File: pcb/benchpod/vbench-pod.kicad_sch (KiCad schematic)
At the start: 112 parts, among them J1 PZ254V-12-22P, SW1 TS-1088-AR02016, SW2 TS-1088-AR02016, U1 ICE40UP5K-SG48ITR, U10 TCAN1044VDRBRQ1, U2 W25Q64JVSSIQ, U24 SN74LVC2G66DCUR, U4 ESP32-C3-MINI-1-N4, U5 STM32H563ZIT6, U7 APS6404L-3SQR-ZR, U8 TPS2116DRLR, X1 SX3M48.000B10F20TNN, Y2 Crystal_GND24

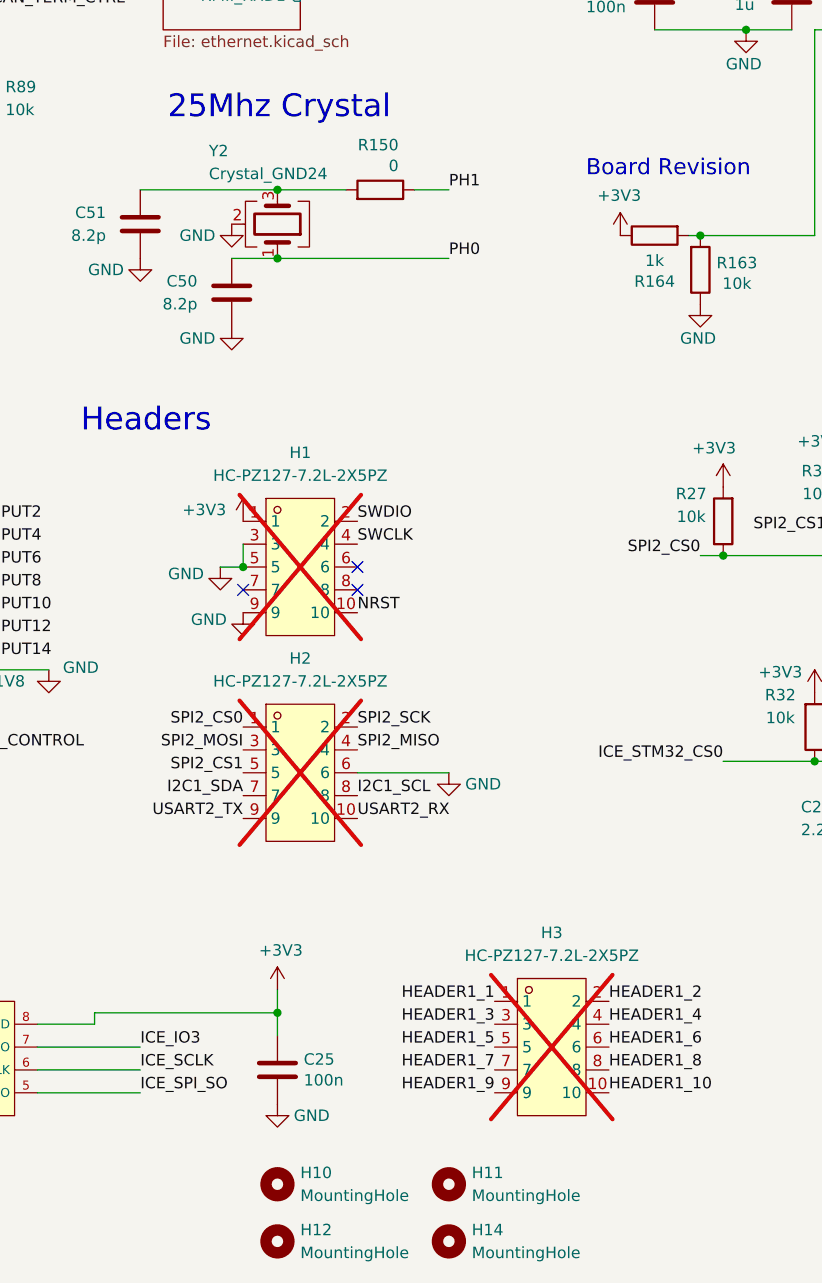
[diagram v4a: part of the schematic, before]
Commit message: replace d1, cleanups, cap changes
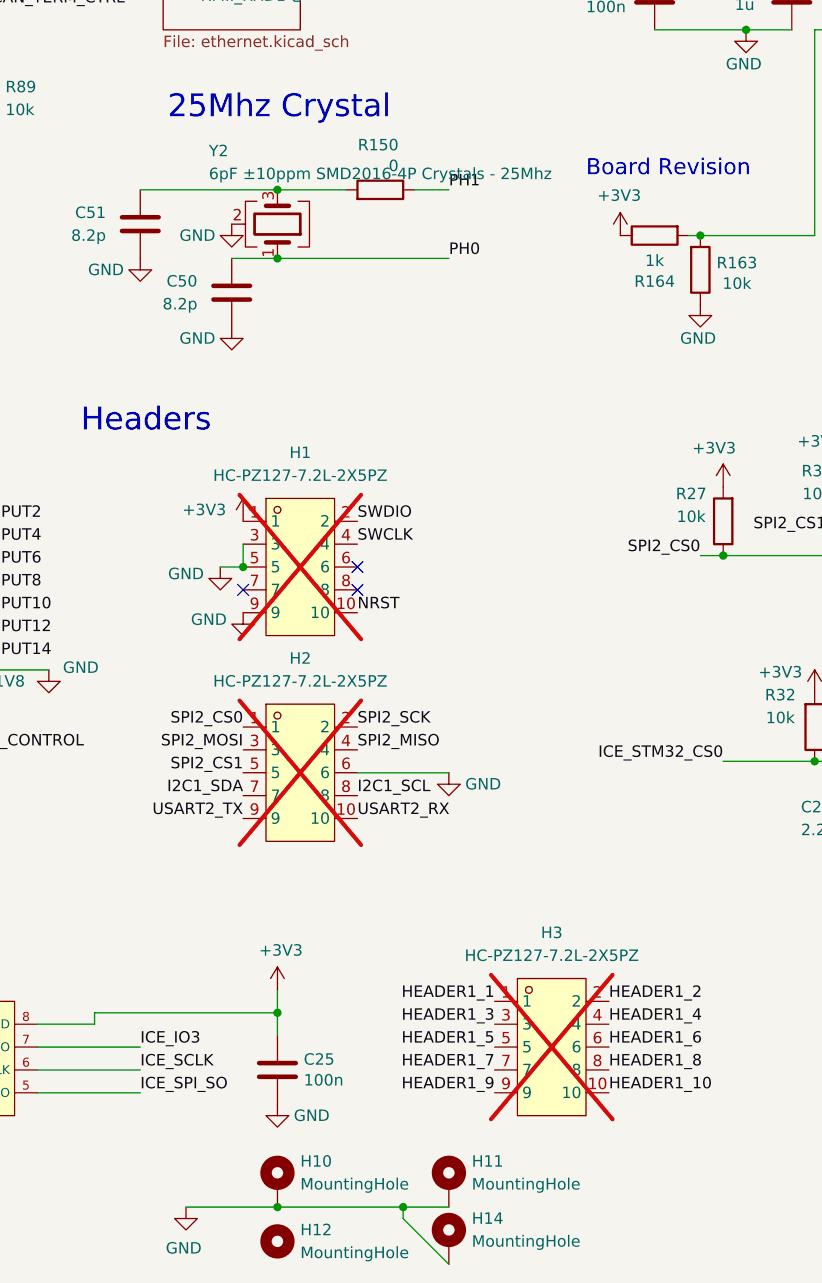
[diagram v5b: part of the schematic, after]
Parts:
- C2, C3: footprint Capacitor_SMD:C_0603_1608Metric -> Capacitor_SMD:C_0805_2012Metric; LCSC C19666 -> C98192
- C220: footprint Capacitor_SMD:C_1206_3216Metric -> Capacitor_SMD:C_0805_2012Metric; LCSC C29823 -> C98192
- H10, H11, H14: footprint MountingHole:MountingHole_2.7mm_M2.5 -> MountingHole:MountingHole_2.7mm_M2.5_Pad_Via; symbol Mechanical:MountingHole -> Mechanical:MountingHole_Pad
- Y2: value Crystal_GND24 -> 6pF ±10ppm SMD2016-4P Crystals - 25Mhz
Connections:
- net GND: now also H10.1, H11.1, H14.1
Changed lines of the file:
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@@
 	)
 	(junction
+		(at 246.38 275.59)
+		(diameter 0)
+		(color 0 0 0 0)
+	)
+	(junction
+		(at 260.35 275.59)
+		(diameter 0)
+		(color 0 0 0 0)
+	)
+	(junction
 		(at 323.85 36.83)
 		(diameter 0)
@@
 	(wire
 		(pts
+			(xy 236.22 275.59) (xy 246.38 275.59)
+		)
+		(stroke
+			(width 0)
+			(type default)
+		)
+	)
+	(wire
+		(pts
 			(xy 40.64 224.79) (xy 39.37 224.79)
 		)
@@
 	(wire
 		(pts
+			(xy 260.35 275.59) (xy 265.43 275.59)
+		)
+		(stroke
+			(width 0)
+			(type default)
+		)
+	)
+	(wire
+		(pts
 			(xy 196.85 62.23) (xy 196.85 64.77)
 		)
@@
 	(wire
 		(pts
+			(xy 246.38 275.59) (xy 260.35 275.59)
+		)
+		(stroke
+			(width 0)
+			(type default)
+		)
+	)
+	(wire
+		(pts
 			(xy 306.07 226.06) (xy 330.2 226.06)
 		)
@@
 	(wire
 		(pts
+			(xy 265.43 281.94) (xy 260.35 276.86)
+		)
+		(stroke
+			(width 0)
+			(type default)
+		)
+	)
+	(wire
+		(pts
 			(xy 312.42 36.83) (xy 323.85 36.83)
 		)
@@
 	(wire
 		(pts
+			(xy 260.35 275.59) (xy 260.35 276.86)
+		)
+		(stroke
+			(width 0)
+			(type default)
+		)
+	)
+	(wire
+		(pts
 			(xy 219.71 255.27) (xy 226.06 255.27)
 		)
@@
 	)
 	(symbol
-		(lib_id "Mechanical:MountingHole")
+		(lib_id "Mechanical:MountingHole_Pad")
 		(at 265.43 273.05 0)
 		(unit 1)
@@
 		(fields_autoplaced yes)
 		(property "Reference" "H11"
-			(at 267.97 271.7799 0)
+			(at 267.97 270.5099 0)
 			(show_name no)
 			(do_not_autoplace no)
@@
 		)
 		(property "Value" "MountingHole"
-			(at 267.97 274.3199 0)
+			(at 267.97 273.0499 0)
 			(show_name no)
 			(do_not_autoplace no)
@@
 			)
 		)
-		(property "Footprint" "MountingHole:MountingHole_2.7mm_M2.5"
+		(property "Footprint" "MountingHole:MountingHole_2.7mm_M2.5_Pad_Via"
 			(at 265.43 273.05 0)
 			(hide yes)
@@
 			)
 		)
-		(property "Description" "Mounting Hole without connection"
+		(property "Description" "Mounting Hole with connection"
 			(at 265.43 273.05 0)
 			(hide yes)
@@
 			)
 		)
+		(pin "1"
+		)
 		(instances
 			(project "vbench-pod"
@@
 	)
 	(symbol
+		(lib_id "power:GND")
+		(at 236.22 275.59 0)
+		(unit 1)
+		(body_style 1)
+		(exclude_from_sim no)
+		(in_bom yes)
+		(on_board yes)
+		(in_pos_files yes)
+		(dnp no)
+		(property "Reference" "#PWR064"
+			(at 236.22 281.94 0)
+			(hide yes)
+			(show_name no)
+			(do_not_autoplace no)
+			(effects
+				(font
+					(size 1.27 1.27)
+				)
+			)
+		)
+		(property "Value" "GND"
+			(at 235.966 280.162 0)
+			(show_name no)
+			(do_not_autoplace no)
+			(effects
+				(font
+					(size 1.27 1.27)
+				)
+			)
+		)
+		(property "Footprint" ""
+			(at 236.22 275.59 0)
+			(hide yes)
+			(show_name no)
+			(do_not_autoplace no)
+			(effects
+				(font
+					(size 1.27 1.27)
+				)
+			)
+		)
+		(property "Datasheet" ""
+			(at 236.22 275.59 0)
+			(hide yes)
+			(show_name no)
+			(do_not_autoplace no)
+			(effects
+				(font
+					(size 1.27 1.27)
+				)
+			)
+		)
+		(property "Description" ""
+			(at 236.22 275.59 0)
+			(show_name no)
+			(do_not_autoplace no)
+			(effects
+				(font
+					(size 1.27 1.27)
+				)
+			)
+		)
+		(pin "1"
+		)
+		(instances
+			(project "vbench-pod"
+				(path "/745fcf4b-2e0b-4fc4-95c0-f2e3fd40beb9"
+					(reference "#PWR064")
+					(unit 1)
+				)
+			)
+		)
+	)
+	(symbol
 		(lib_id "Device:C")
 		(at 142.24 30.48 0)
@@
 			)
 		)
-		(property "Footprint" "Capacitor_SMD:C_1206_3216Metric"
+		(property "Footprint" "Capacitor_SMD:C_0805_2012Metric"
 			(at 244.8052 36.83 0)
 			(hide yes)
@@
 			)
 		)
-		(property "LCSC" "C29823"
+		(property "LCSC" "C98192"
 			(at 243.84 33.02 0)
 			(hide yes)
@@
 			)
 		)
-		(property "Footprint" "Capacitor_SMD:C_0603_1608Metric"
+		(property "Footprint" "Capacitor_SMD:C_0805_2012Metric"
 			(at 25.7048 149.86 0)
 			(hide yes)
@@
 			)
 		)
-		(property "LCSC" "C19666"
+		(property "LCSC" "C98192"
 			(at 26.67 146.05 0)
 			(hide yes)
@@
 			)
 		)
-		(property "Value" "Crystal_GND24"
+		(property "Value" "6pF ±10ppm SMD2016-4P Crystals  - 25Mhz"
 			(at 238.76 160.782 90)
 			(show_name no)
@@
 	)
 	(symbol
-		(lib_id "Mechanical:MountingHole")
+		(lib_id "Mechanical:MountingHole_Pad")
 		(at 265.43 279.4 0)
 		(unit 1)
@@
 		(fields_autoplaced yes)
 		(property "Reference" "H14"
-			(at 267.97 278.1299 0)
+			(at 267.97 276.8599 0)
 			(show_name no)
 			(do_not_autoplace no)
@@
 		)
 		(property "Value" "MountingHole"
-			(at 267.97 280.6699 0)
+			(at 267.97 279.3999 0)
 			(show_name no)
 			(do_not_autoplace no)
@@
 			)
 		)
-		(property "Footprint" "MountingHole:MountingHole_2.7mm_M2.5"
+		(property "Footprint" "MountingHole:MountingHole_2.7mm_M2.5_Pad_Via"
 			(at 265.43 279.4 0)
 			(hide yes)
@@
 			)
 		)
-		(property "Description" "Mounting Hole without connection"
+		(property "Description" "Mounting Hole with connection"
 			(at 265.43 279.4 0)
 			(hide yes)
@@
 			)
 		)
+		(pin "1"
+		)
 		(instances
 			(project "vbench-pod"
@@
 	)
 	(symbol
-		(lib_id "Mechanical:MountingHole")
+		(lib_id "Mechanical:MountingHole_Pad")
 		(at 246.38 273.05 0)
 		(unit 1)
@@
 		(fields_autoplaced yes)
 		(property "Reference" "H10"
-			(at 248.92 271.7799 0)
+			(at 248.92 270.5099 0)
 			(show_name no)
 			(do_not_autoplace no)
@@
 		)
 		(property "Value" "MountingHole"
-			(at 248.92 274.3199 0)
+			(at 248.92 273.0499 0)
 			(show_name no)
 			(do_not_autoplace no)
@@
 			)
 		)
-		(property "Footprint" "MountingHole:MountingHole_2.7mm_M2.5"
+		(property "Footprint" "MountingHole:MountingHole_2.7mm_M2.5_Pad_Via"
 			(at 246.38 273.05 0)
 			(hide yes)
@@
 			)
 		)
-		(property "Description" "Mounting Hole without connection"
+		(property "Description" "Mounting Hole with connection"
 			(at 246.38 273.05 0)
 			(hide yes)
@@
 			)
 		)
+		(pin "1"
+		)
 		(instances
 			(project "vbench-pod"
@@
 			)
 		)
-		(property "Footprint" "Capacitor_SMD:C_0603_1608Metric"
+		(property "Footprint" "Capacitor_SMD:C_0805_2012Metric"
 			(at 28.2448 135.89 0)
 			(hide yes)
@@
 			)
 		)
-		(property "LCSC" "C19666"
+		(property "LCSC" "C98192"
 			(at 29.21 132.08 0)
 			(hide yes)

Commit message: 5VA->5V for relays, resistor and cap changes
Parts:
- removed C59: 100n, Capacitor_SMD:C_0402_1005Metric, symbol Device:C
- removed FB1: FerriteBead, lcsc:L0603, symbol Device:FerriteBead
- added C66: 10u, Capacitor_SMD:C_0603_1608Metric, symbol Device:C
- added C97: 100n, Capacitor_SMD:C_0402_1005Metric, symbol Device:C
- added R174: 330, Resistor_SMD:R_0402_1005Metric, symbol Device:R
- added R175: 1k, Resistor_SMD:R_0402_1005Metric, symbol Device:R
- added R176: 56, Resistor_SMD:R_0402_1005Metric, symbol Device:R
- added R177: 100, Resistor_SMD:R_0402_1005Metric, symbol Device:R
- added U28: SRV05-4.TCT, lcsc:SOT-23-6_L2.9-W1.6-P0.95-LS2.8-BR, symbol edward_lib:SRV05-4.TCT
- C5: value 1u -> 4.7u; footprint Capacitor_SMD:C_0402_1005Metric -> Capacitor_SMD:C_0805_2012Metric; KiLib_Generator SMD_2terminal_chip_molded -> (none); LCSC C1518208 -> C98192; MPN CL21B105KBFNNNE -> (none)
- R18: value 120 -> 56; LCSC C25079 -> C25127
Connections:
- net +3V3: now also U8.5 (MODE), C97.2, U28.5
- net 1V2: now also C48.2, U1.30 (VCC), U1.5 (VCC), R177.2
- net CAN+: now also R176.1; no longer U24.1 (1A)
- net GND: now also C66.2, C97.1, R175.1, U28.2; no longer U8.5 (MODE)
- net LA_VCCIO: now also C66.1, R175.2
- net NRST_CONTROL: now also R174.1, U28.3; no longer U5.14 (PF4)
- net at C5.2, C6.2, U1.29 (VCCPLL): now also R177.1; no longer C48.2, U1.30 (VCC), U1.5 (VCC)
- net PD7: no longer names the net of U5.123 (PD7)
- net PG10: no longer names the net of U5.125 (PG10)
- net PG9: no longer names the net of U5.124 (PG9)
- new net: R174.2, U5.14 (PF4)
- new net: R176.2, U24.1 (1A)
- no-connect marks 56 -> 62
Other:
- note added: "bleeder resistor"
- moved on the sheet: C1, C2, C3, C4, C5, C6, J1

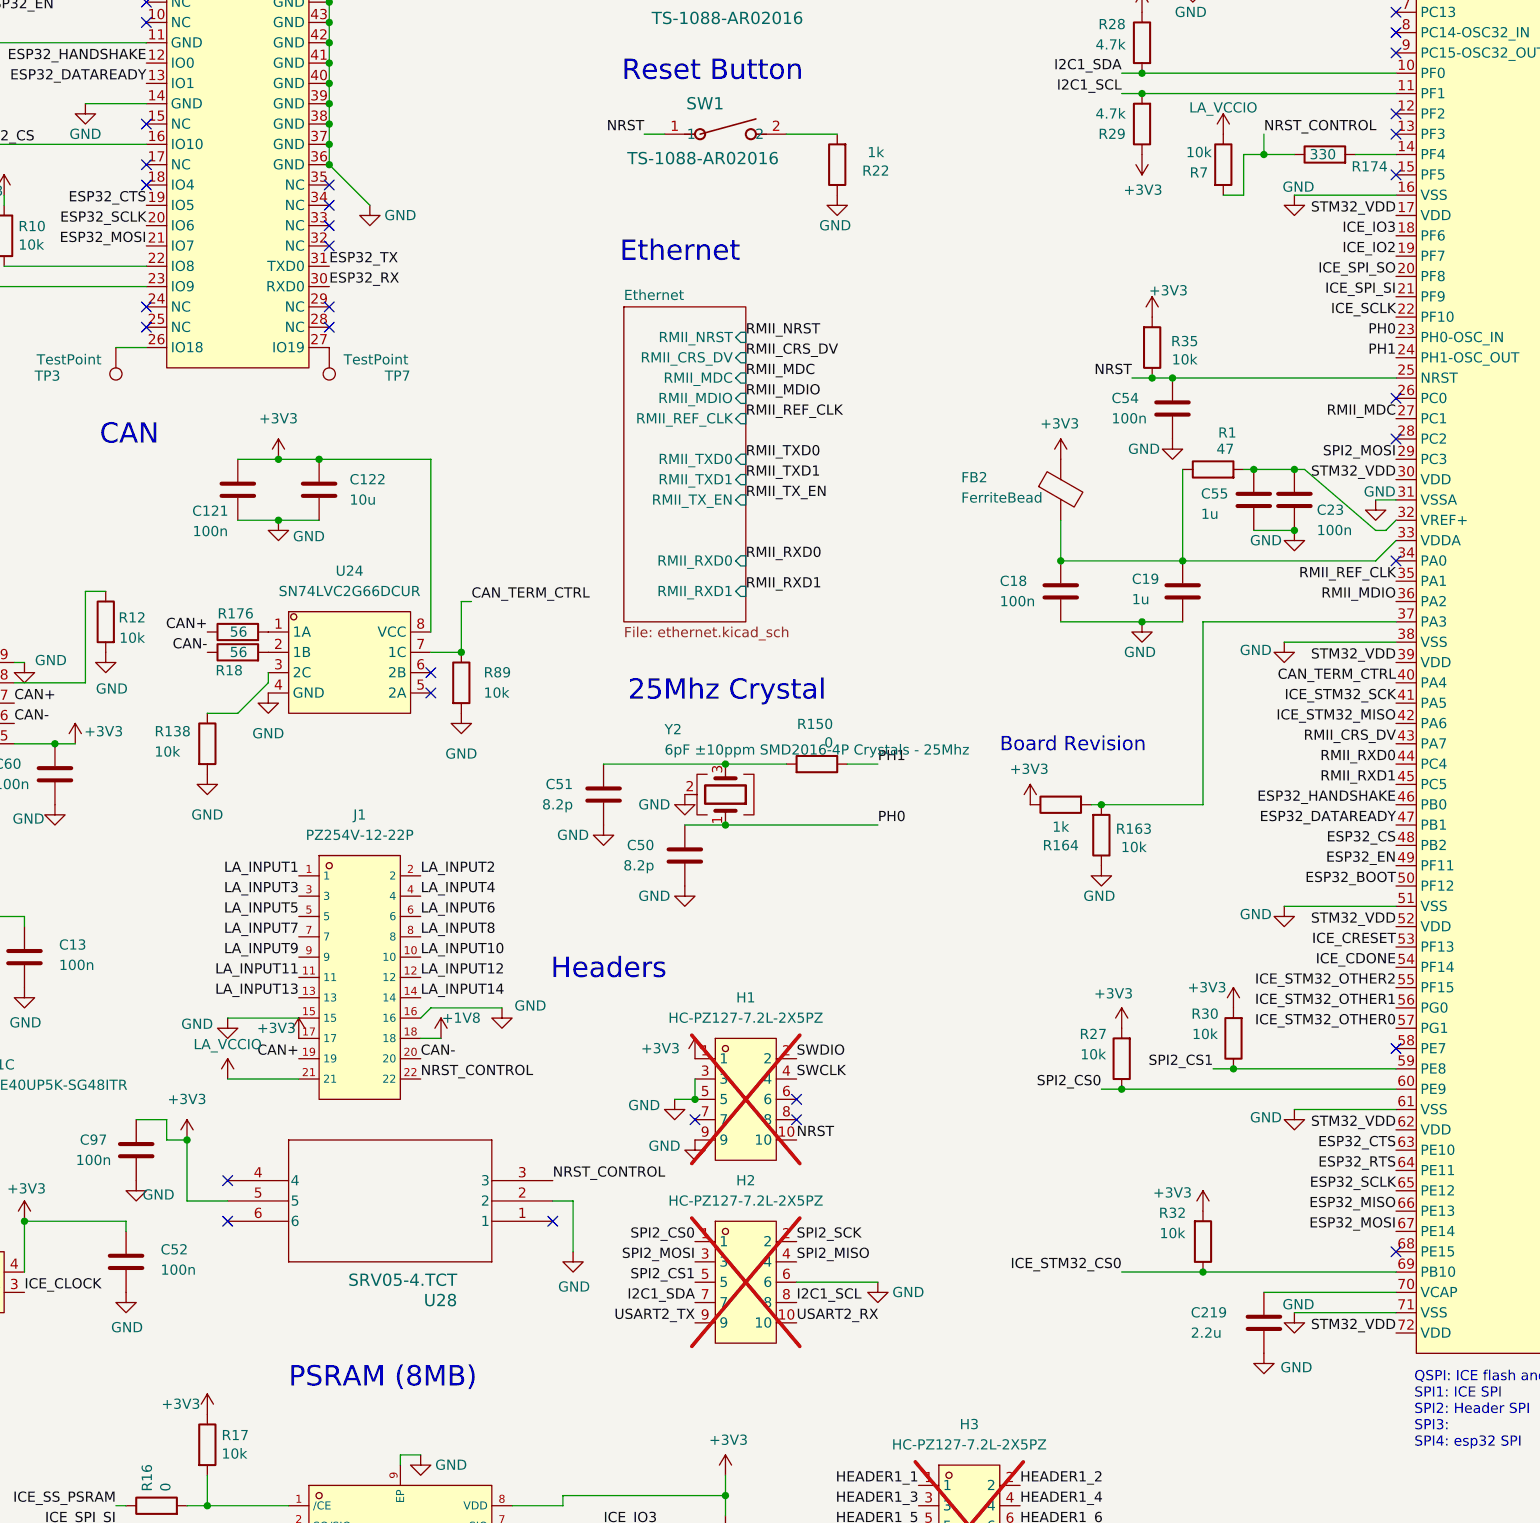
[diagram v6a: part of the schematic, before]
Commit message: 5VA->5V for relays rerouting
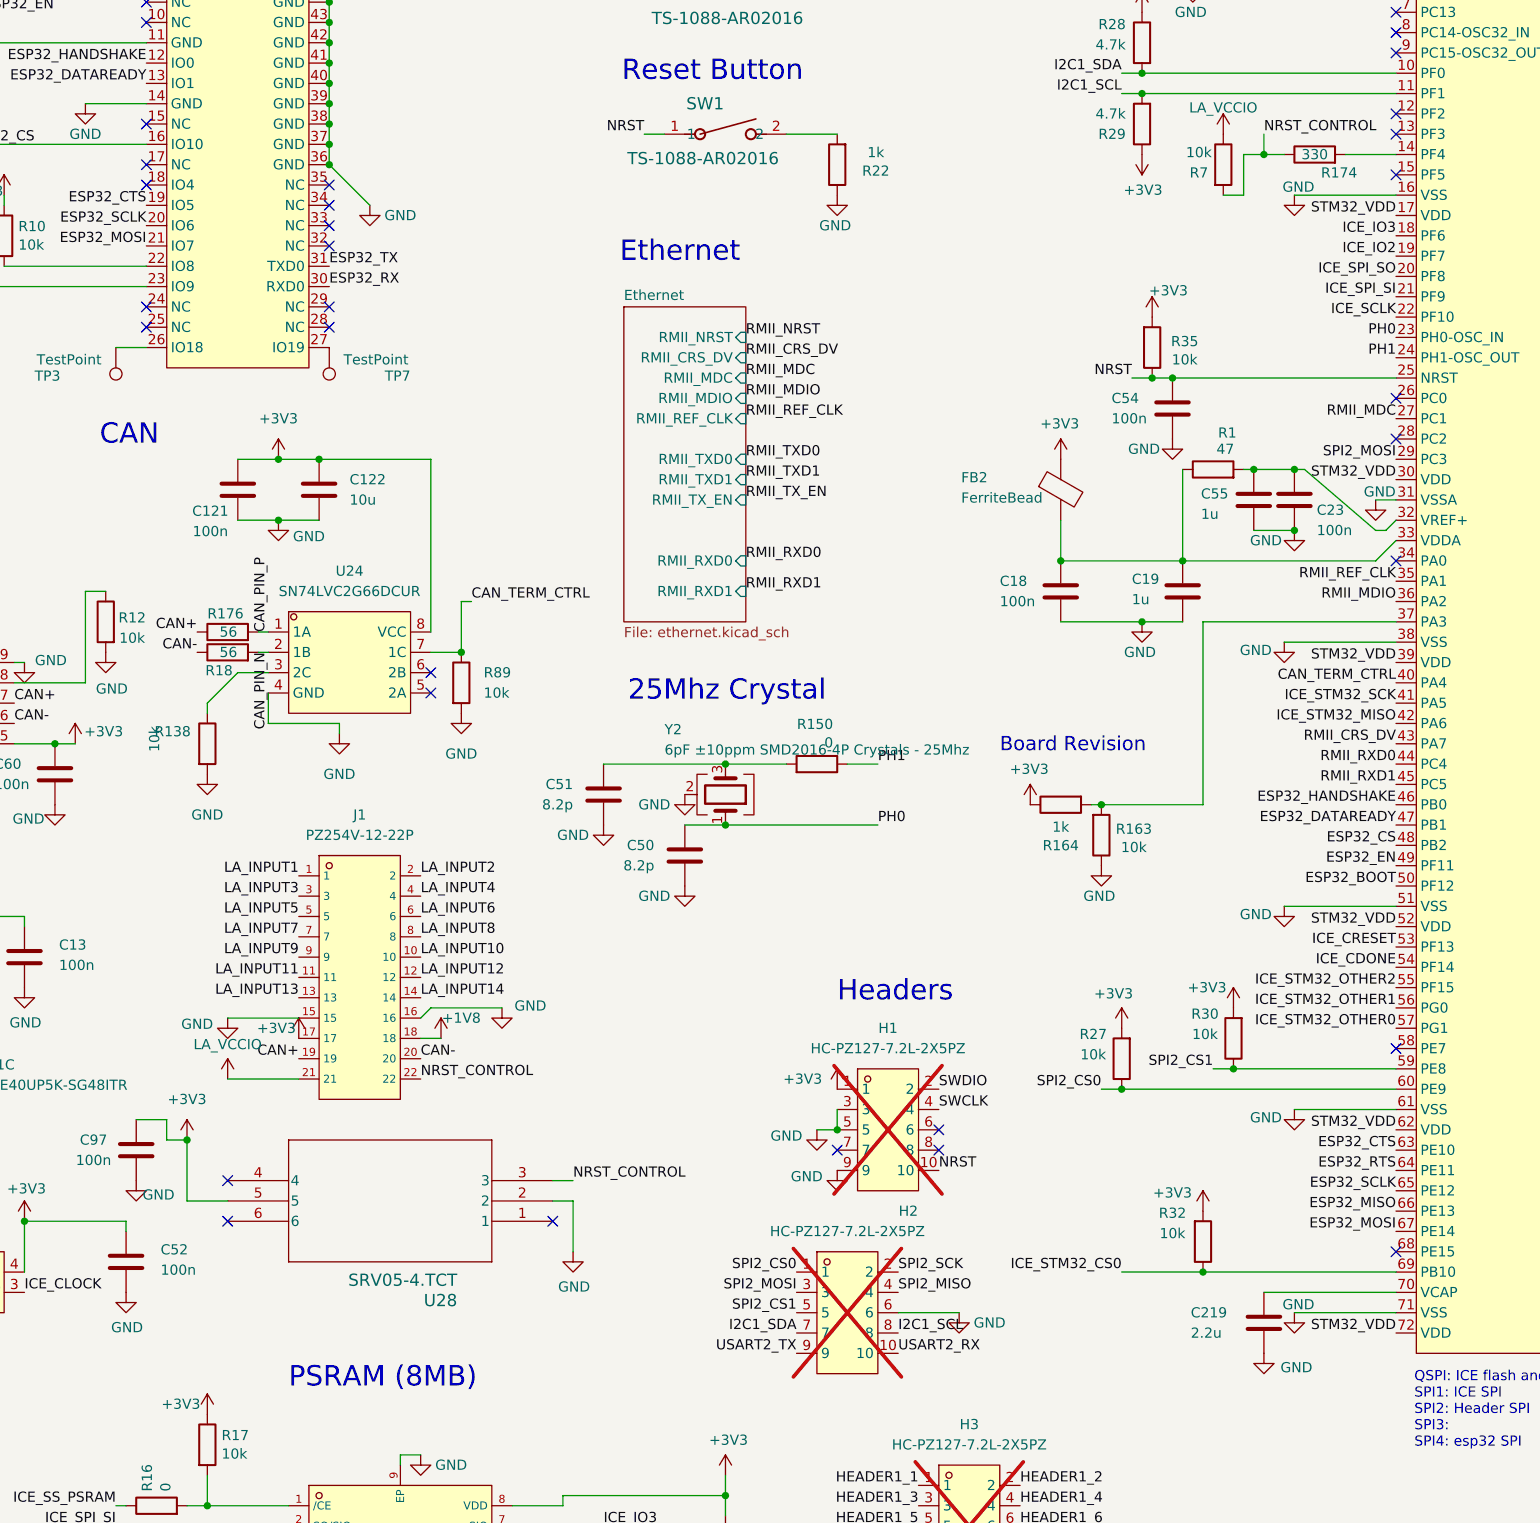
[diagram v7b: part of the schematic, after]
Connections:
- net CAN_PIN_P: now reaches R176.2, U24.1 (1A)
- net CAN_PIN_N: now reaches R18.2, U24.2 (1B)
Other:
- moved on the sheet: H1, H2, R176, R18
